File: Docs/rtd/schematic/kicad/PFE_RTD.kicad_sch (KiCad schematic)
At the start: 10 parts, among them U1 LM741cn

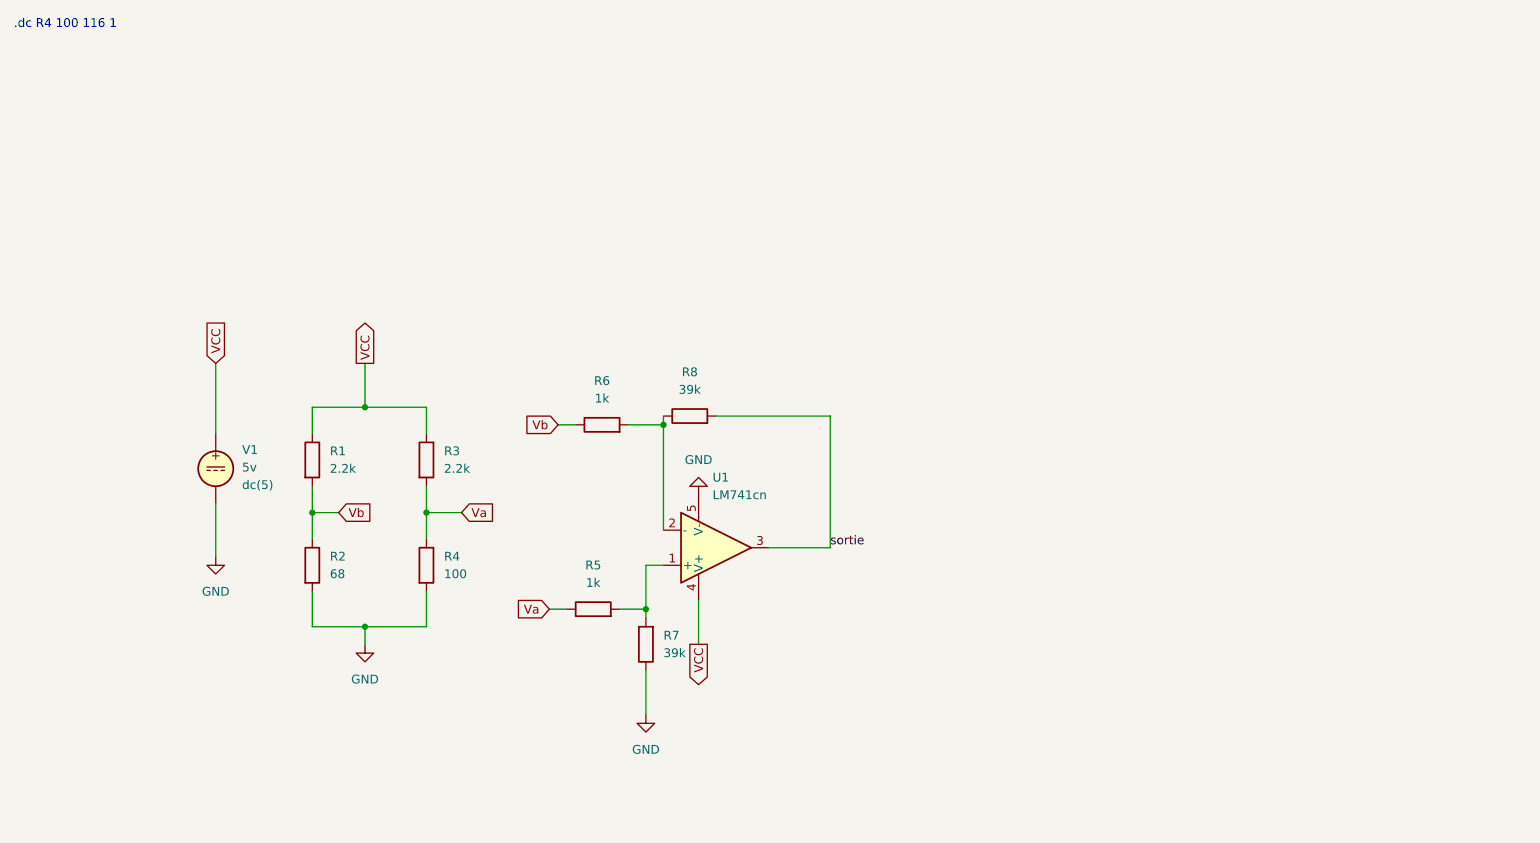
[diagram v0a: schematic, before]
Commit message: comment added in main.ino; revision 0.1 RTD PT100 schematic
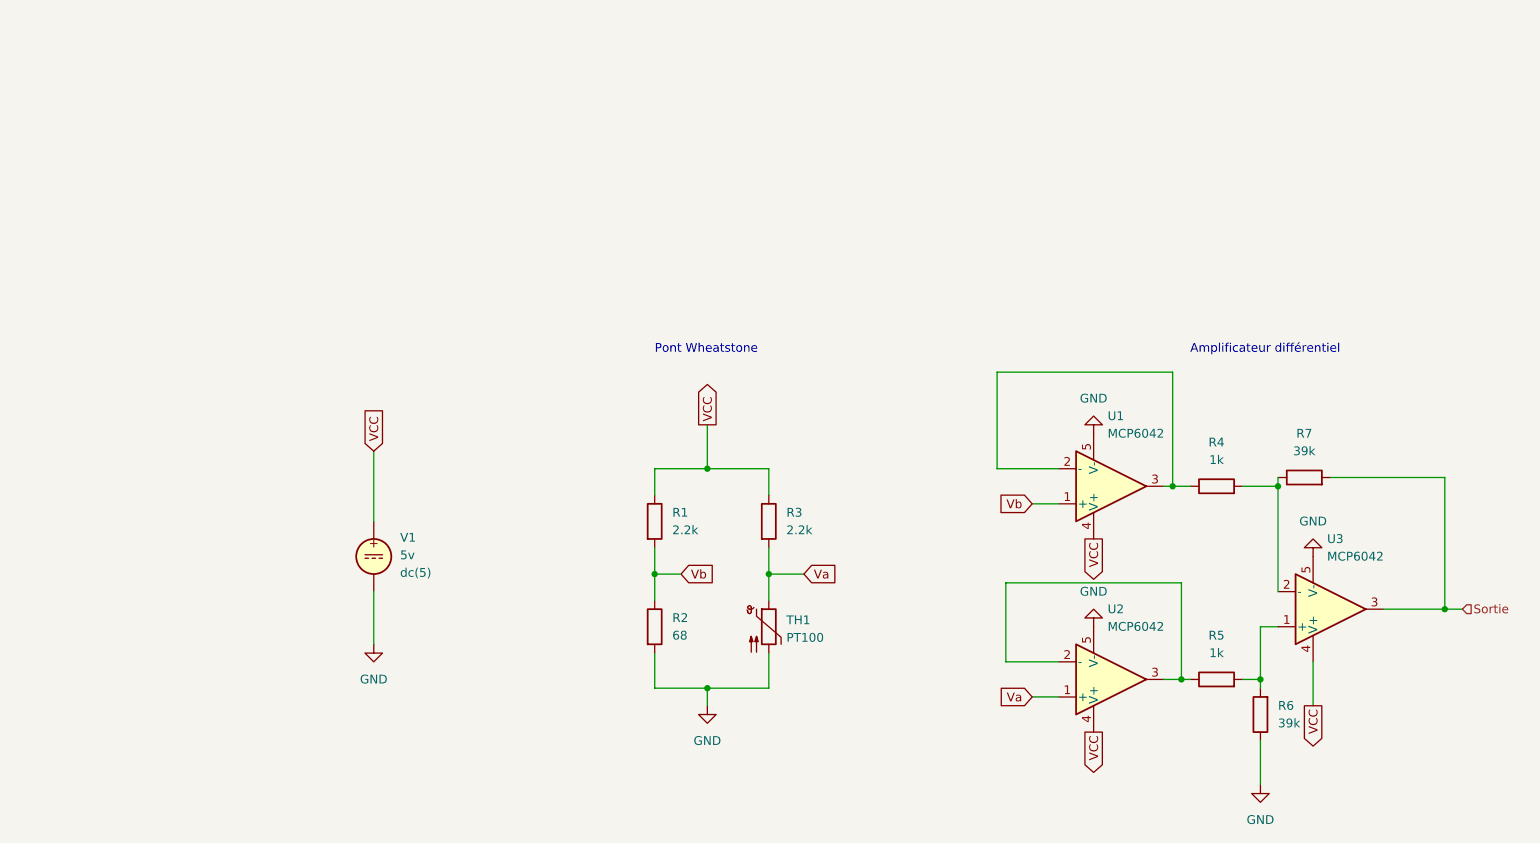
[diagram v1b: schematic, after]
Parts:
- removed R4: 100, symbol Device:R
- added TH1: PT100, symbol Sensor_Temperature:PT100
- added U1, U2: MCP6042, symbol pspice:OPAMP
- U3: renamed from U1; value LM741cn -> MCP6042; Spice_Lib_File LM741cn/lm741.lib -> MCP604x/MCP6041.txt; Spice_Model LM741 -> MCP6041
- renumbered R6 to R4, R7 to R6, R8 to R7
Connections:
- net GND: now also TH1.2, U1.5 (V-), U2.5 (V-)
- net VCC: now also U1.4 (V+), U2.4 (V+)
- net Va: now also TH1.1, U2.1 (+); no longer R5.1
- net Vb: now also U1.1 (+); no longer R4.1
- net sortie renamed Sortie
- new net: R5.1, U2.2 (-), U2.3
- new net: R4.1, U1.2 (-), U1.3
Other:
- note added: "Amplificateur différentiel"
- note added: "Pont Wheatstone"
- note removed: ".dc R4 100 116 1"
- company: (none) -> ÉTS - PFE HIVER 2022 - ELE795
- title: (none) -> RTD PT100 - Circuit d'adaptation
- moved on the sheet: R1, R2, R3, R4, R5, R6, R7, U3, V1
